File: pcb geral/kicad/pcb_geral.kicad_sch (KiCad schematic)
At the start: 6 parts, among them J1 ESP32 Connector_1, J2 ESP32 Connector_2, J3 Keyboard Connector_1, J4 Keyboard Connector_2, J5 Flat Cable Header, J6 FLAT CABLE SOCKET

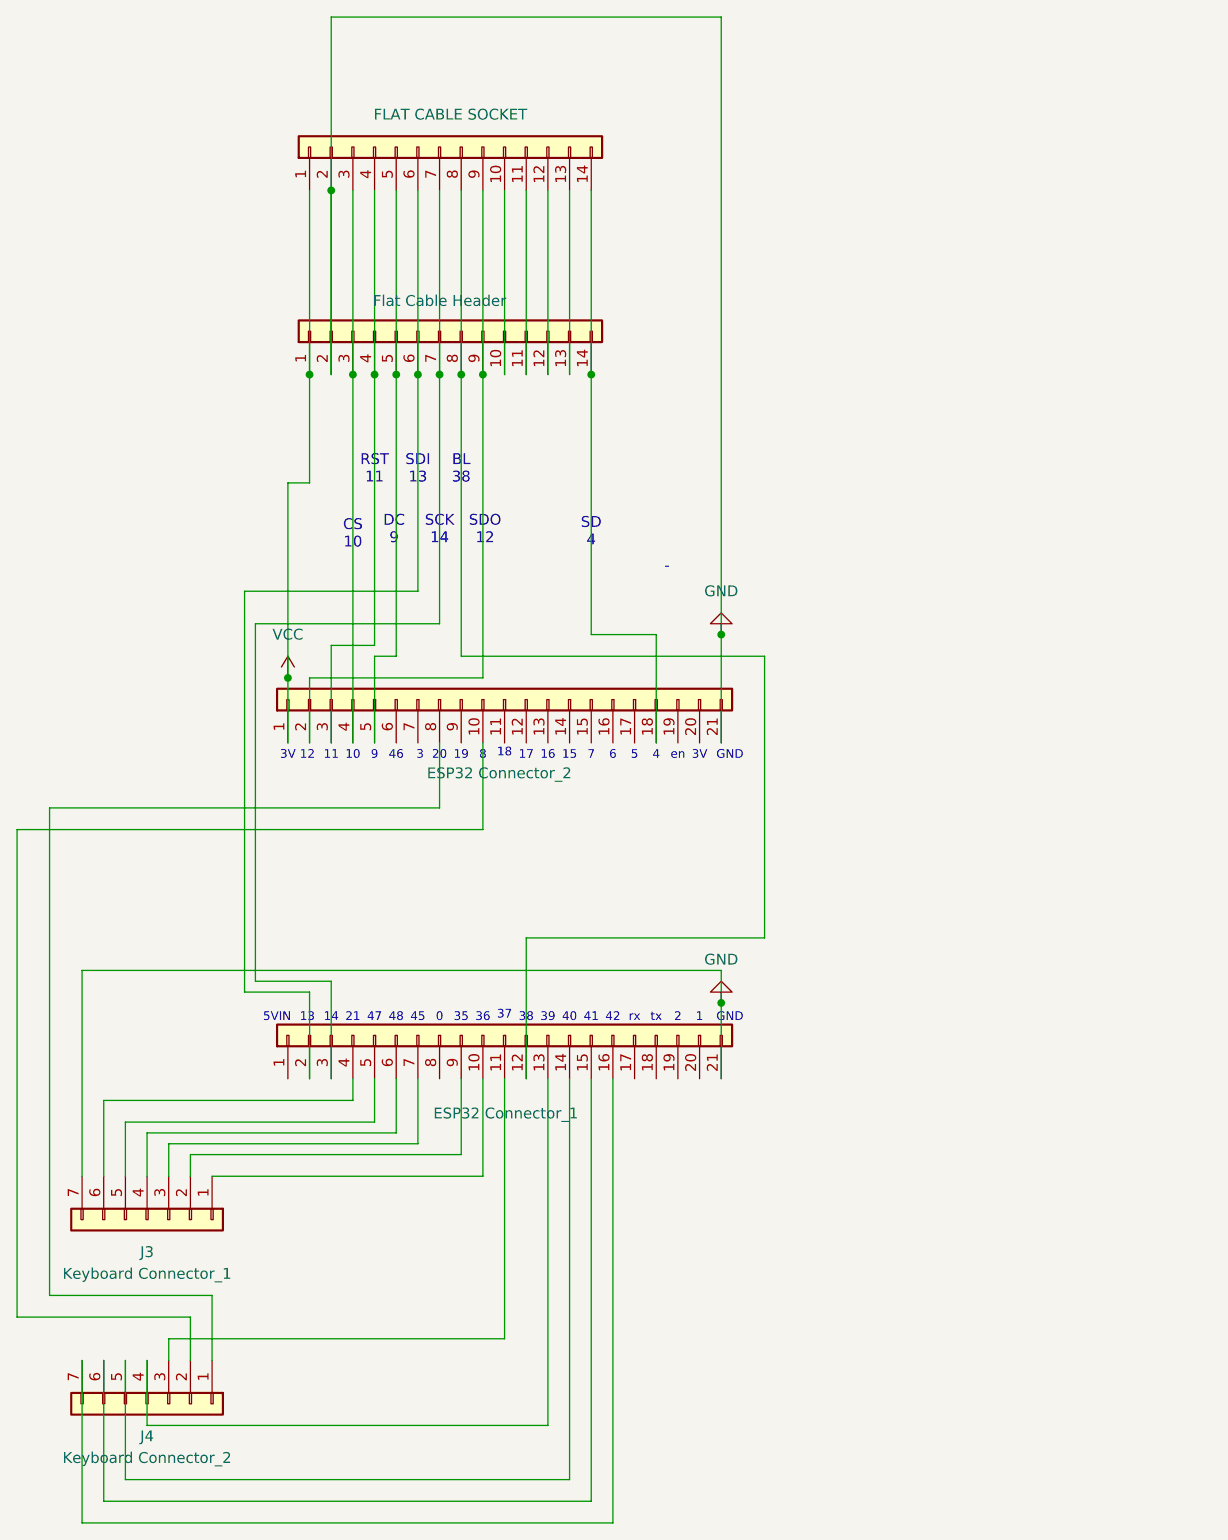
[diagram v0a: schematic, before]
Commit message: Added Battery Holder to BOM and modified PCB schematic
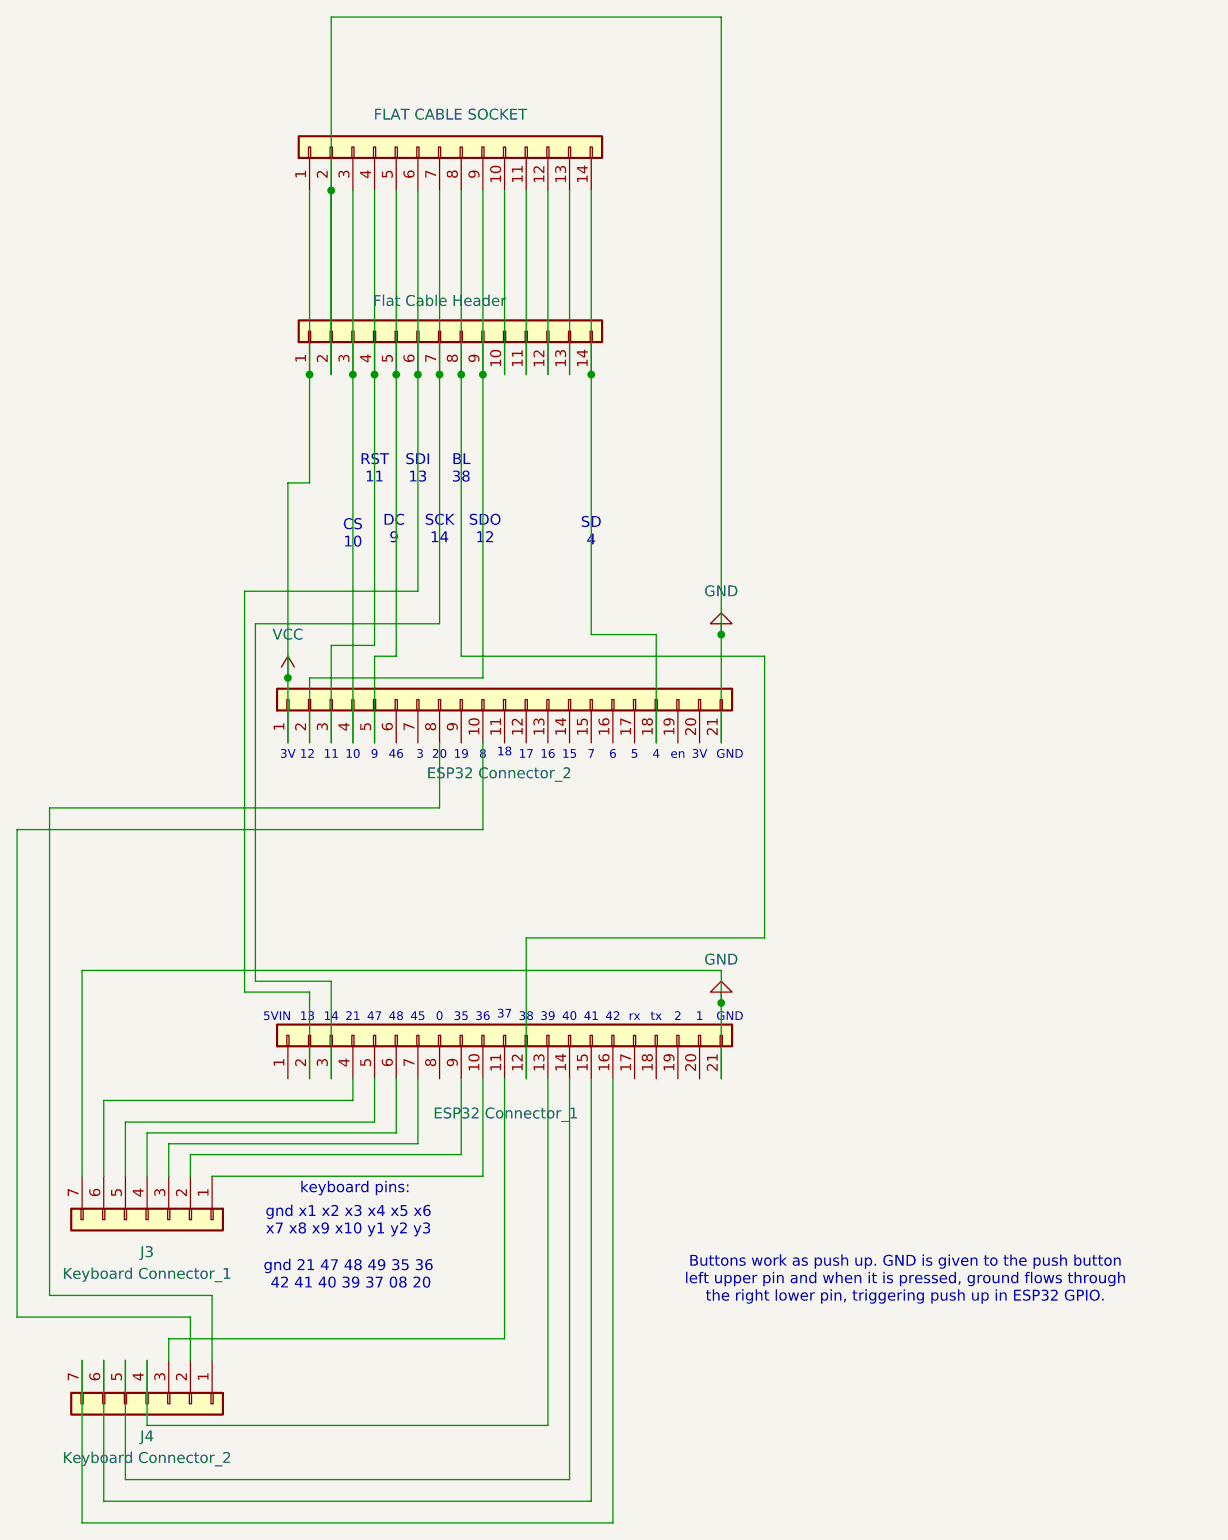
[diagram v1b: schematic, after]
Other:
- note added: "Buttons work as push up. GND is given to the push button left upper pin and when it is pressed, ground flows through the right lower pin, triggering push up in ESP32 GPIO."
- note added: "gnd 21 47 48 49 35 36 42 41 40 39 37 08 20"
- note added: "gnd x1 x2 x3 x4 x5 x6 x7 x8 x9 x10 y1 y2 y3"
- note added: "keyboard pins:"
- note removed: "-"
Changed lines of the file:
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@@
+		)
+	)
+	(text "Buttons work as push up. GND is given to the push button \nleft upper pin and when it is pressed, ground flows through\nthe right lower pin, triggering push up in ESP32 GPIO."
+		(exclude_from_sim no)
+		(at 118.11 162.052 0)
+		(effects
+			(font
+				(size 1.27 1.27)
+			)
 		)
 	)
@@
 		)
 	)
-	(text "-\n"
-		(exclude_from_sim no)
-		(at 90.17 78.486 0)
-		(effects
-			(font
-				(size 1.27 1.27)
-			)
-		)
-	)
 	(text "7"
 		(exclude_from_sim no)
@@
 		)
 	)
+	(text "keyboard pins:"
+		(exclude_from_sim no)
+		(at 53.594 151.384 0)
+		(effects
+			(font
+				(size 1.27 1.27)
+			)
+		)
+	)
 	(text "14"
 		(exclude_from_sim no)
@@
 			)
 		)
+	)
+	(text "gnd 21 47 48 49 35 36\n 42 41 40 39 37 08 20"
+		(exclude_from_sim no)
+		(at 52.832 161.544 0)
+		(effects
+			(font
+				(size 1.27 1.27)
+			)
+		)
+	)
+	(text "gnd x1 x2 x3 x4 x5 x6\nx7 x8 x9 x10 y1 y2 y3"
+		(exclude_from_sim no)
+		(at 52.832 155.194 0)
+		(effects
+			(font
+				(size 1.27 1.27)
+			)
+		)

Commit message: Updated cart and schematics
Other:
- note added: "Keyboard will be connected using pin headers and sockets"
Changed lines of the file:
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@@
+		)
+	)
+	(text "Keyboard will be connected using pin headers and sockets"
+		(exclude_from_sim no)
+		(at 117.602 173.99 0)
+		(effects
+			(font
+				(size 1.27 1.27)
+			)
 		)
 	)
@@
 		)
 		(property "Value" "ESP32 Connector_1"
-			(at 79.756 142.494 90)
-			(effects
-				(font
+			(at 80.264 128.524 90)
+			(effects
+				(font
